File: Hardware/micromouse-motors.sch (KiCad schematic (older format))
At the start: 5 parts

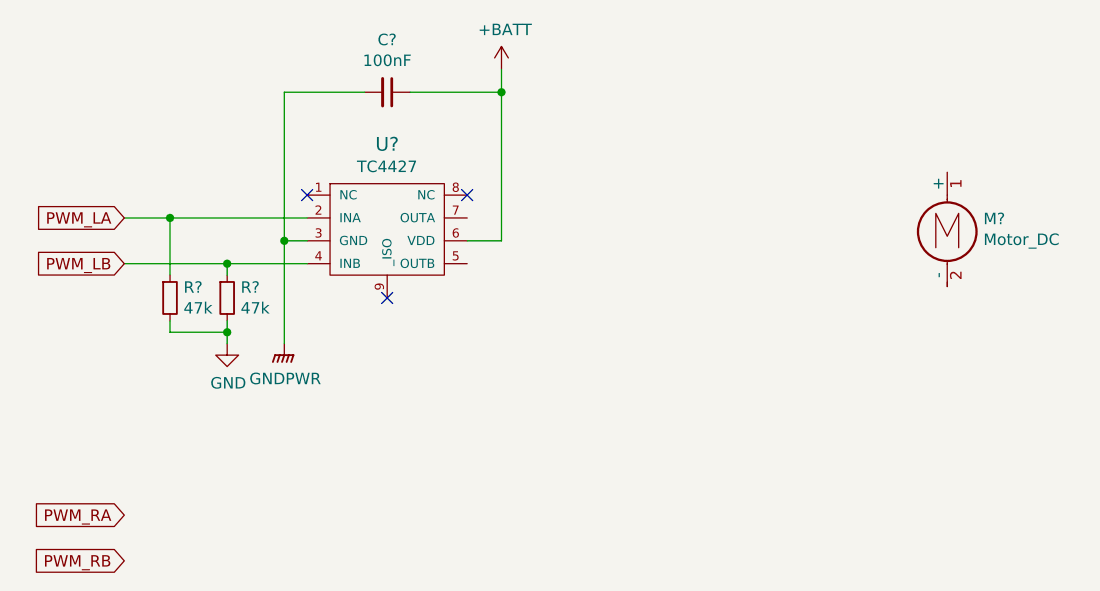
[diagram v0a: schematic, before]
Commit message: add power sub-schematic, fix some supply-connections, rearrange sub-schematics
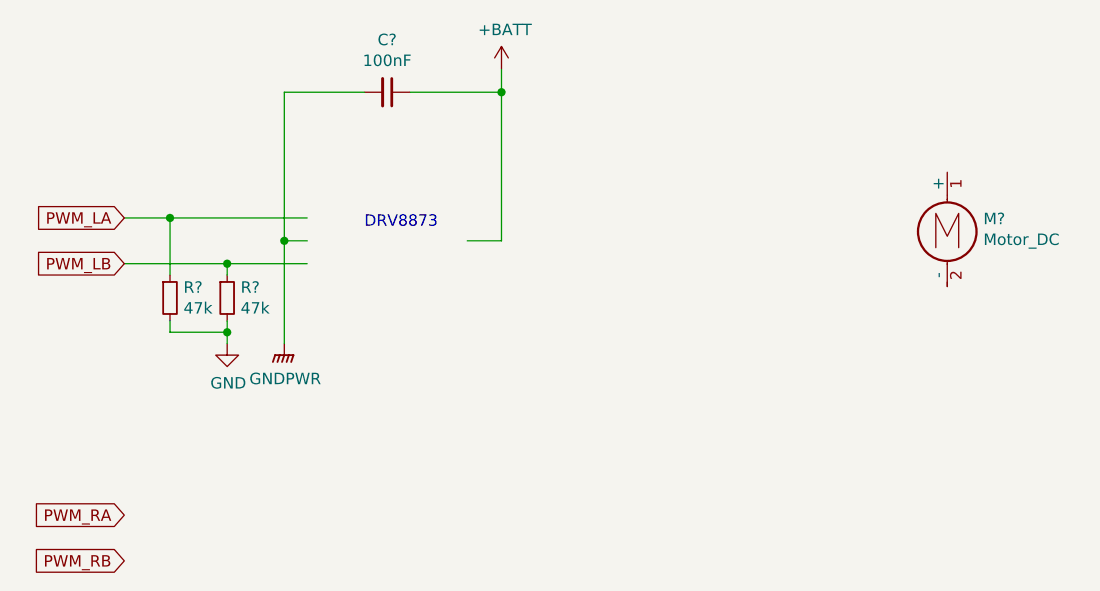
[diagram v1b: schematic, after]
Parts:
- removed U?: TC4427, symbol tc4427:TC4427
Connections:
- no-connect marks 3 -> 0
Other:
- note added: "DRV8873"
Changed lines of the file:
@@
 $Descr A4 11693 8268
 encoding utf-8
-Sheet 6 7
+Sheet 6 8
 Title ""
 Date ""
@@
 Comment4 ""
 $EndDescr
-$Comp
-L tc4427:TC4427 U?
-U 1 1 5CBF5C67
-P 4750 3850
-F 0 "U?" H 4750 4222 60  0000 C CNN
-F 1 "TC4427" H 4750 4124 50  0000 C CNN
-F 2 "" H 4750 3850 60  0000 C CNN
-F 3 "" H 4750 3850 60  0000 C CNN
-	1    4750 3850
-	1    0    0    -1
-$EndComp
 $Comp
 L power:+BATT #PWR?
@@
 Wire Wire Line
 	3800 3800 4400 3800
-NoConn ~ 4400 3700
-NoConn ~ 5100 3700
 Wire Wire Line
 	4300 3900 4300 3250
@@
 	5250 3250 5250 3150
 Connection ~ 5250 3250
-NoConn ~ 4750 4150
 $Comp
 L power:GNDPWR #PWR?
@@
 Text GLabel 3600 5300 0    50   Input ~ 0
 PWM_RB
+Text Notes 4650 3850 0    50   ~ 0
+DRV8873
 $EndSCHEMATC
